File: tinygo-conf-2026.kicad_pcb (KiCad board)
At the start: 2 copper layers, 98 x 70 mm, 19 parts, among them J1 Conn_01x04_Pin, J2 Conn_01x03_Pin, J3 Conn_01x08_Pin, SW1 SW_Push, SW2 SW_Push, U2 RKJXV122400R, U3 adafruit-MAX98357

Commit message: フットプリントライブラリとシンボルのファイル追加と更新
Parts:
- removed U1: ~, espressif:ESP32-S3-DevKitC_ZigZag
- added U4: ESP32-S3-Devkit, origin:ESP32-S3-DevKitC_ZigZag, B.Cu at (121.1, 81.3)
- J3: footprint ST7789:ST7789_1.3_240x240_LCD_Module_Zigzag -> ST7789:ST7789_1.3_240x240_LCD_Module

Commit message: ファイルを追加してリネーム
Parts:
- added G***: LOGO, gopher:scaled_chip_gopher, F.Cu at (101.4, 149.0)
- added G***: LOGO, gopher:scaled_chip_gopher2, F.Cu at (182.8, 149.0)
- added J4: AHT21B, Connector_PinHeader_2.54mm:PinHeader_1x04_P2.54mm_Vertical, F.Cu at (175.9, 128.8)
- added J5: Conn_02x08_Counter_Clockwise, Connector_PinSocket_2.54mm:PinSocket_2x08_P2.54mm_Vertical, B.Cu at (130.6, 164.6)
- added QR*****: https://github.com/tinygo-keeb/tinygo-conf-2026-badge, origin:tinygo-conf-badge-qr-code, B.Cu at (138.9, 145.5)
- moved REF** 27.9 mm to (117.5, 164.5)
- moved REF** 27.9 mm to (161.0, 164.5)
- moved D3 27.7 mm to (182.8, 164.7)
- moved D4 27.7 mm to (95.2, 164.7)
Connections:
- U4 pad 13: unconnected-(U4-GPIO3-Pad13) -> /GPIO3
- U4 pad 25: unconnected-(U4-GPIO19-Pad25) -> /SCL_AHT21B
- U4 pad 26: unconnected-(U4-GPIO20-Pad26) -> /SDA_AHT21B
- U4 pad 32: unconnected-(U4-GPIO35-Pad32) -> /GPIO35
- U4 pad 33: unconnected-(U4-GPIO36-Pad33) -> /GPIO36
- U4 pad 34: unconnected-(U4-GPIO37-Pad34) -> /GPIO37
- U4 pad 35: unconnected-(U4-GPIO38-Pad35) -> /GPIO38
- U4 pad 36: unconnected-(U4-GPIO39/MTCK-Pad36) -> /GPIO39
- U4 pad 37: unconnected-(U4-GPIO40/MTDO-Pad37) -> /GPIO40
- U4 pad 38: unconnected-(U4-GPIO41/MTDI-Pad38) -> /GPIO41
- U4 pad 39: unconnected-(U4-GPIO42/MTMS-Pad39) -> /GPIO42
- U4 pad 40: unconnected-(U4-GPIO2-Pad40) -> /GPIO2
- U4 pad 41: unconnected-(U4-GPIO1-Pad41) -> /GPIO1
- U4 pad 44: unconnected-(U4-GND-Pad44) -> GND
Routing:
- net /GPIO3: track 0.00 -> 88.1 mm, vias 0 -> 2
- net /GPIO2: track 0.00 -> 71.2 mm, vias 0 -> 1
- net /GPIO35: track 0.00 -> 70.0 mm, vias 0 -> 1
- net VCC: track 113.8 -> 181.2 mm
- net /GPIO1: track 0.00 -> 64.4 mm, vias 0 -> 1
- net /GPIO36: track 0.00 -> 61.7 mm, vias 0 -> 1
- net /GPIO41: track 0.00 -> 58.8 mm, vias 0 -> 1
- net /GPIO39: track 0.00 -> 58.4 mm, vias 0 -> 1
- net /GPIO37: track 0.00 -> 58.3 mm, vias 0 -> 1
- net /GPIO42: track 0.00 -> 58.1 mm, vias 0 -> 1
- net /GPIO40: track 0.00 -> 58.1 mm, vias 0 -> 1
- net /GPIO38: track 0.00 -> 58.0 mm, vias 0 -> 1
- net /SCL_AHT21B: track 0.00 -> 44.6 mm, vias 0 -> 2
- net /3V3: track 305.8 -> 344.3 mm, vias 0 -> 2
- net /SDA_AHT21B: track 0.00 -> 34.3 mm, vias 0 -> 1
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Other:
- board size 98 x 70 mm -> 98 x 98 mm
- board text added: "+"
- board text added: "-"
- board text added: "01"
- board text added: "02"
- board text added: "03"
- board text added: "04"
- board text added: "36"
- board text added: "37"
- board text added: "38"
- board text added: "39"
- board text added: "3v3"
- board text added: "40"
- board text added: "41"
- board text added: "42"
- board text added: "5v"
- board text added: "GND"
- board text added: "TinyGo Conference 2026"
- board text removed: "TEST TEST TEST"

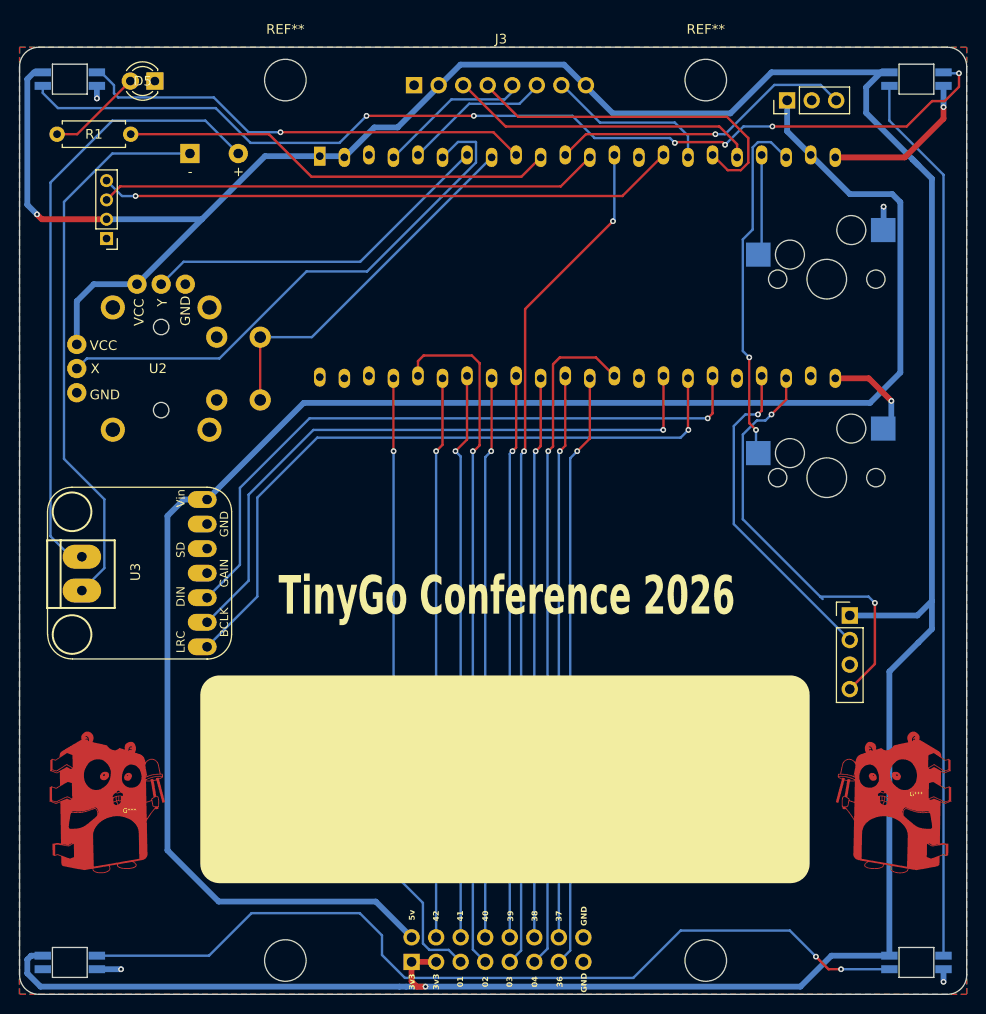
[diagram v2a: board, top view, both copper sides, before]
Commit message: 配線変更と基板の穴を追加
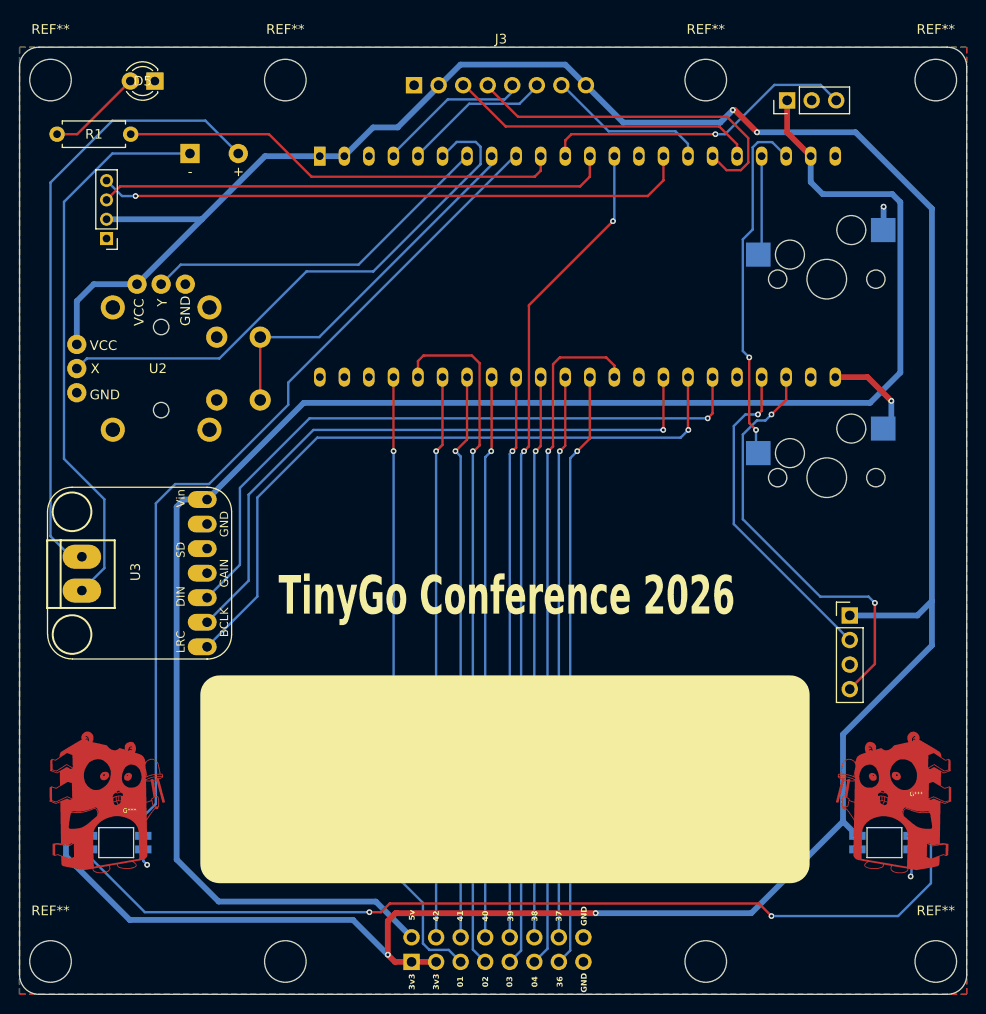
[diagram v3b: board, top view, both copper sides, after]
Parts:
- removed D3, D4: WS2812B, kbd:YS-SK6812MINI-E
- added REF**: MountingHole_4.3mm_M4, MountingHole:MountingHole_4.3mm_M4, F.Cu at (184.8, 73.4)
- added REF**: MountingHole_4.3mm_M4, MountingHole:MountingHole_4.3mm_M4, F.Cu at (93.2, 73.4)
- added REF**: MountingHole_4.3mm_M4, MountingHole:MountingHole_4.3mm_M4, F.Cu at (184.8, 164.6)
- added REF**: MountingHole_4.3mm_M4, MountingHole:MountingHole_4.3mm_M4, F.Cu at (93.2, 164.6)
- U4: footprint origin:ESP32-S3-DevKitC_ZigZag -> espressif:ESP32-S3-DevKitC
- moved D1 79.1 mm to (100.0, 152.3)
- moved D2 79.1 mm to (179.5, 152.3)
- moved REF** 0.10 mm to (117.5, 164.6)
- moved REF** 0.10 mm to (161.0, 164.6)
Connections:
- D2 pad 2: Net-(D2-DOUT) -> unconnected-(D2-DOUT-Pad2)
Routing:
- net Net-(D2-DOUT): track 92.3 -> 0.00 mm
- net Net-(D3-DOUT): track 91.5 -> 0.00 mm, vias 2 -> 0
- net /3V3: track 344.3 -> 300.6 mm, vias 2 -> 4
- net /LED: track 47.4 -> 88.5 mm, vias 1 -> 0
- net GND: track 33.8 -> 17.1 mm, vias 6 -> 4
- net Net-(D1-DOUT): track 105.7 -> 99.3 mm, vias 6 -> 2
- net /I2C_SCL: track 60.0 -> 61.5 mm
- net /I2C_SDA: track 51.8 -> 53.1 mm
- net /IR_DATA: track 31.7 -> 32.7 mm
- net /IR_LED: track 45.1 -> 46.0 mm
- net VCC: track 181.2 -> 182.0 mm
- net /GPIO35: track 70.0 -> 70.7 mm
- net /VR_Y: track 56.4 -> 57.1 mm
- net /CS: track 17.6 -> 16.9 mm
- net /VR_BTN: track 38.1 -> 38.7 mm

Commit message: 温湿度センサーのGPIOがUSBとかぶっていたので変更
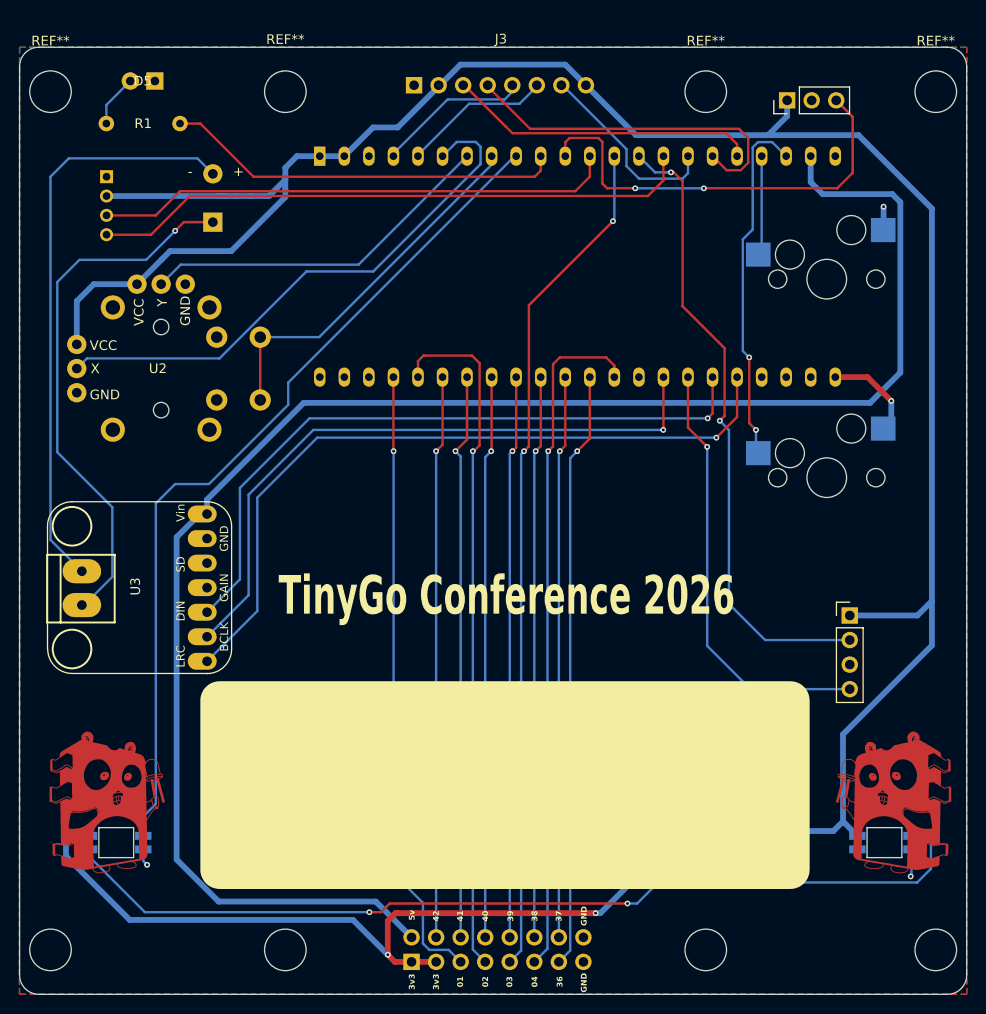
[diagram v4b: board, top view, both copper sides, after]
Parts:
- moved LS1 7.49 mm to (110.0, 88.1), turned to 90 degrees
- moved J1 6.40 mm to (99.0, 83.4), turned to 0 degrees
- moved R1 5.22 mm to (106.6, 77.9)
- moved U3 1.50 mm to (102.5, 125.8)
- moved REF** 1.20 mm to (184.8, 74.6)
- moved REF** 1.20 mm to (117.5, 163.4)
- moved REF** 1.20 mm to (93.2, 74.6)
- moved REF** 1.20 mm to (184.8, 163.4)
- moved REF** 1.20 mm to (161.0, 74.6)
- moved REF** 1.20 mm to (93.2, 163.4)
- moved REF** 1.20 mm to (117.5, 74.6)
- moved REF** 1.20 mm to (161.0, 163.4)
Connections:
- J2 pad 1: VCC -> /3V3
- U4 pad 14: unconnected-(U4-GPIO46-Pad14) -> /SDA_AHT21B
- U4 pad 25: /SCL_AHT21B -> unconnected-(U4-GPIO19-Pad25)
- U4 pad 26: /SDA_AHT21B -> unconnected-(U4-GPIO20-Pad26)
- U4 pad 27: unconnected-(U4-GPIO21-Pad27) -> /LRC
- U4 pad 29: /LRC -> /SCL_AHT21B
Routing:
- net /SDA_AHT21B: track 34.1 -> 65.8 mm, vias 1 -> 2
- net /3V3: track 300.6 -> 315.7 mm, vias 4 -> 2
- net /IR_DATA: track 32.7 -> 44.9 mm, vias 1 -> 2
- net VCC: track 182.0 -> 174.3 mm
- net /LRC: track 70.6 -> 76.3 mm
- net /IR_LED: track 46.0 -> 41.4 mm
- net Net-(D5-A): track 9.86 -> 5.43 mm
- net Net-(U3-OUTN): track 64.2 -> 60.4 mm
- net /CS: track 16.9 -> 20.2 mm
- net Net-(U3-OUTP): track 58.0 -> 55.9 mm, vias 0 -> 1
- net Net-(D1-DOUT): track 99.3 -> 97.3 mm
- net /DIN: track 68.6 -> 70.1 mm
- net /BCLK: track 66.1 -> 67.6 mm
- net /SCL_AHT21B: track 44.2 -> 45.2 mm, vias 2 -> 1
- net /I2C_SCL: track 61.5 -> 62.5 mm, vias 1 -> 0
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
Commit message: PSRAM用のGPIOを使わないように再配線
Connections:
- J4 pad 2: /SDA_AHT21B -> /GPIO41
- J4 pad 4: /SCL_AHT21B -> /GPIO42
- J5 pad 10: /GPIO37 -> /GPIO40
- J5 pad 11: /GPIO38 -> /GPIO41
- J5 pad 12: /GPIO39 -> /GPIO42
- J5 pad 13: /GPIO40 -> /BCLK
- J5 pad 14: /GPIO41 -> /GPIO46
- J5 pad 15: /GPIO42 -> /GPIO48
- J5 pad 6: /GPIO35 -> /GPIO38
- J5 pad 7: /GPIO36 -> /GPIO39
- U4 pad 14: /SDA_AHT21B -> /GPIO46
- U4 pad 29: /SCL_AHT21B -> /GPIO48
- U4 pad 32: /GPIO35 -> unconnected-(U4-GPIO35-Pad32)
- U4 pad 33: /GPIO36 -> unconnected-(U4-GPIO36-Pad33)
- U4 pad 34: /GPIO37 -> unconnected-(U4-GPIO37-Pad34)
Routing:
- net /GPIO46: track 0.00 -> 105.5 mm, vias 0 -> 1
- net /GPIO48: track 0.00 -> 84.4 mm, vias 0 -> 1
- net /GPIO35: track 70.7 -> 0.00 mm, vias 1 -> 0
- net /SDA_AHT21B: track 65.8 -> 0.00 mm, vias 2 -> 0
- net /GPIO36: track 61.8 -> 0.00 mm, vias 1 -> 0
- net /BCLK: track 67.6 -> 128.0 mm, vias 1 -> 2
- net /GPIO37: track 58.1 -> 0.00 mm, vias 1 -> 0
- net /GPIO42: track 58.2 -> 115.6 mm, vias 1 -> 2
- net /GPIO41: track 58.7 -> 109.9 mm, vias 1 -> 3
- net /SCL_AHT21B: track 45.2 -> 0.00 mm, vias 1 -> 0
- net GND: track 17.1 -> 31.7 mm, vias 4 -> 3
- net /GPIO38: track 58.0 -> 68.2 mm
- net /GPIO2: track 71.3 -> 63.4 mm
- net /GPIO39: track 58.2 -> 63.5 mm
- net /GPIO3: track 88.0 -> 91.8 mm
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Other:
- board text added: "45"
- board text added: "46"
- board text added: "48"
- board text added: "GPIO35"
- board text added: "GPIO37"
- board text removed: "+"
- board text removed: "-"
- board text removed: "04"
- board text removed: "36"
- board text removed: "37"
